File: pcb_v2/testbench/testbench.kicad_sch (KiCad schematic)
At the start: 68 parts, among them J1 test_A, J10 test_C1, J11 test_C2, J12 test_C3, J15 lcd, J17 DEBUG, J18 power_jack, J2 test_B, J3 sub_0, J4 sub_8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

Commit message: projeto enviado para impressao em dezembro/25
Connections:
- net +5V: now also J9.3 (Pin_3)
- net test_0: no longer J10.1 (Pin_1)
- net test_25: now also J10.4 (Pin_4)
- net test_26: now also J10.6 (Pin_6)
- net test_27: now also J10.8 (Pin_8)
- net test_28: now also J10.10 (Pin_10)
- net test_29: now also J10.12 (Pin_12)
- net test_30: now also J10.14 (Pin_14)
- net test_7: no longer J10.15 (Pin_15)
- net test_power_gnd_C: now also J10.15 (Pin_15); no longer J10.10 (Pin_10), J10.12 (Pin_12), J10.14 (Pin_14)
- net test_power_vcc: now also J10.1 (Pin_1); no longer J10.4 (Pin_4), J10.6 (Pin_6), J10.8 (Pin_8)
- no-connect marks 55 -> 54

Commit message: versao B2 da testbench (com a alimentacao das placas de teste reposicionadas para as extremidades
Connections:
- net mcu_power_scl: now also J9.6 (Pin_6); no longer J9.5 (Pin_5)
- net mcu_power_sda: now also J9.5 (Pin_5); no longer J9.6 (Pin_6)
- net test_0: no longer J1.1 (Pin_1), J2.1 (Pin_1)
- net test_13: no longer J1.14 (Pin_14)
- net test_21: no longer J2.22 (Pin_22)
- net test_24: no longer J1.15 (Pin_15), J2.23 (Pin_23)
- net test_31: now also J2.30 (Pin_30)
- net test_32: now also J1.23 (Pin_23), J2.31 (Pin_31)
- net test_33: now also J1.24 (Pin_24)
- net test_37: no longer J1.28 (Pin_28)
- net test_45: no longer J2.44 (Pin_44)
- net test_7: now also J2.8 (Pin_8)
- net test_8: now also J1.9 (Pin_9), J2.9 (Pin_9)
- net test_9: now also J1.10 (Pin_10)
- net test_power_gnd_A: now also J1.14 (Pin_14), J1.28 (Pin_28); no longer J1.10 (Pin_10), J1.24 (Pin_24)
- net test_power_gnd_B: now also J2.22 (Pin_22), J2.44 (Pin_44); no longer J2.31 (Pin_31), J2.9 (Pin_9)
- net test_power_vcc: now also J1.1 (Pin_1), J1.15 (Pin_15), J2.1 (Pin_1), J2.23 (Pin_23); no longer J1.23 (Pin_23), J1.9 (Pin_9), J2.30 (Pin_30), J2.8 (Pin_8)

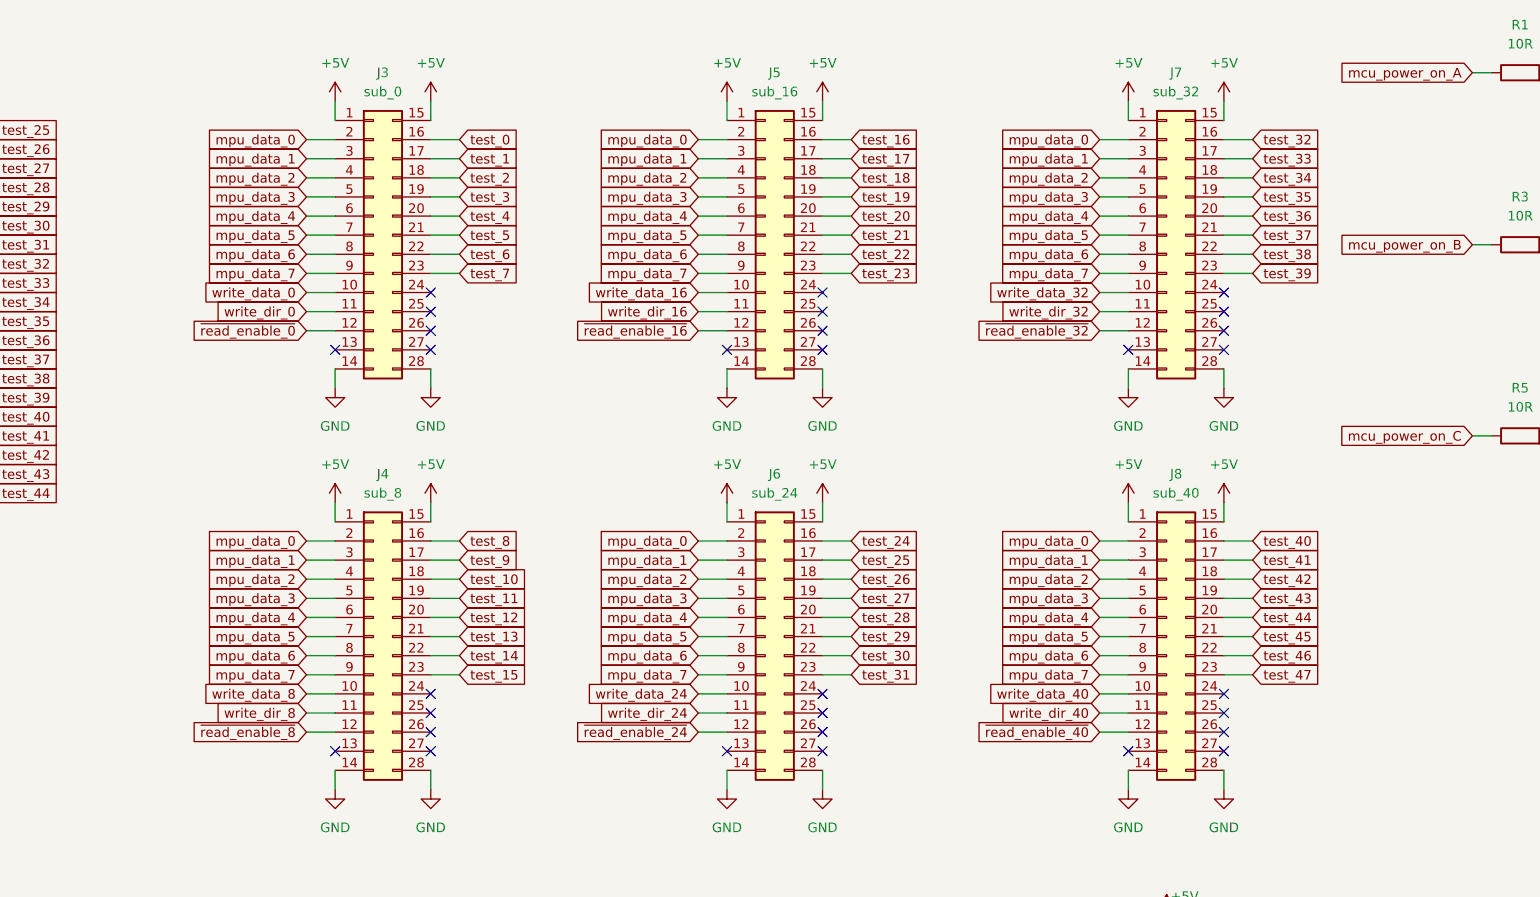
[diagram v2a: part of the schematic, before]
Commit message: a interface com a sub8 parece incompativel; corrigindo a interface
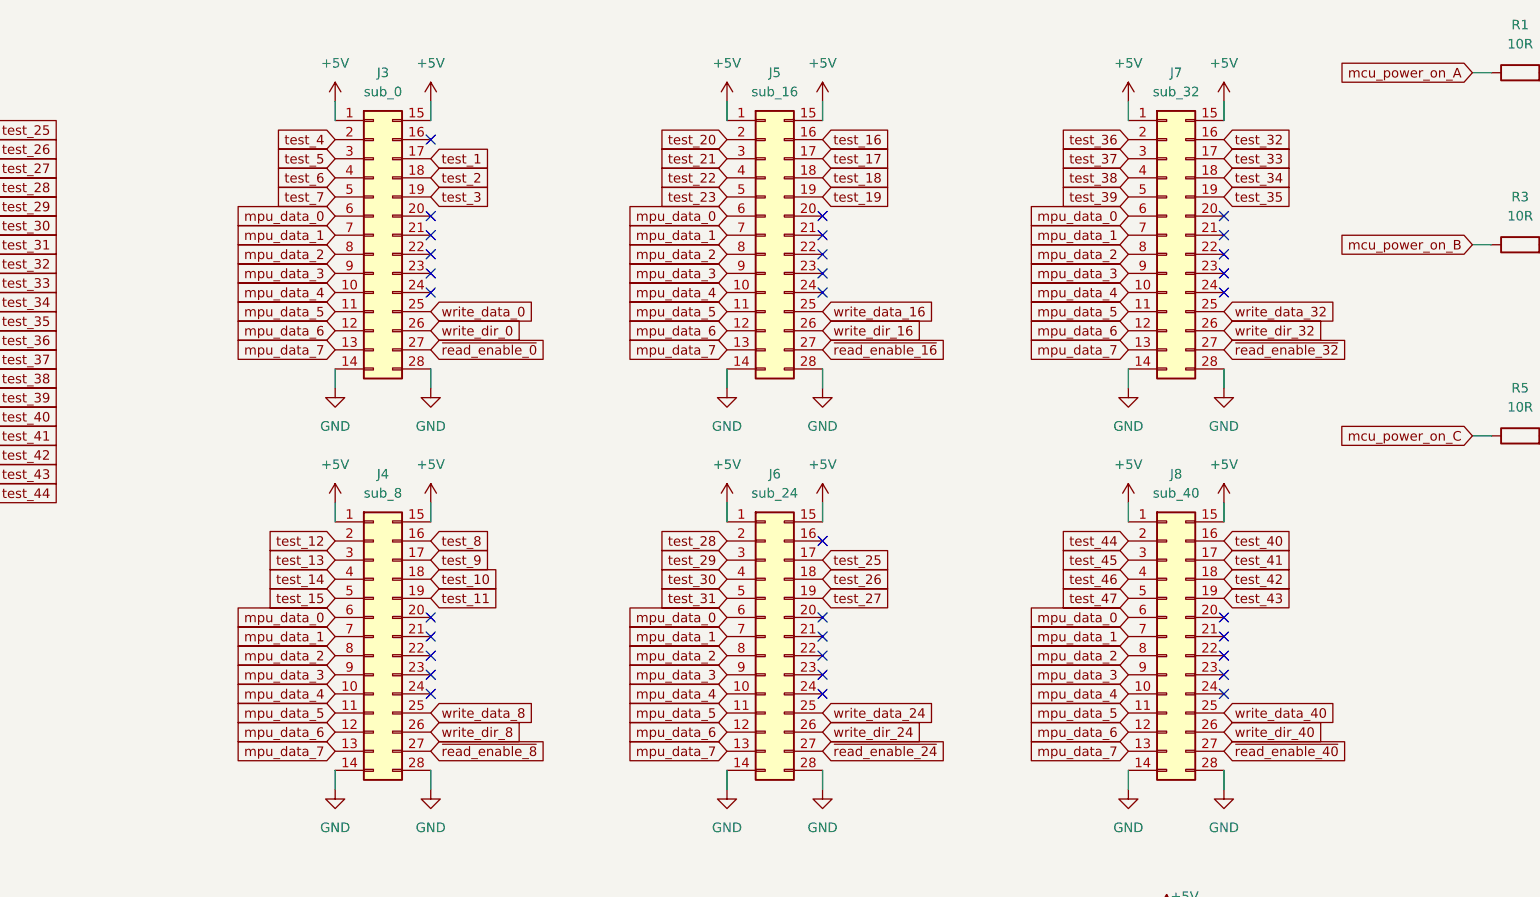
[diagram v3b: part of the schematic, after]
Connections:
- net mpu_data_0: now also J3.6 (Pin_6), J4.6 (Pin_6), J5.6 (Pin_6), J6.6 (Pin_6), J7.6 (Pin_6), J8.6 (Pin_6); no longer J3.2 (Pin_2), J4.2 (Pin_2), J5.2 (Pin_2), J6.2 (Pin_2), J7.2 (Pin_2), J8.2 (Pin_2)
- net mpu_data_1: now also J3.7 (Pin_7), J4.7 (Pin_7), J5.7 (Pin_7), J6.7 (Pin_7), J7.7 (Pin_7), J8.7 (Pin_7); no longer J3.3 (Pin_3), J4.3 (Pin_3), J5.3 (Pin_3), J6.3 (Pin_3), J7.3 (Pin_3), J8.3 (Pin_3)
- net mpu_data_2: now also J3.8 (Pin_8), J4.8 (Pin_8), J5.8 (Pin_8), J6.8 (Pin_8), J7.8 (Pin_8), J8.8 (Pin_8); no longer J3.4 (Pin_4), J4.4 (Pin_4), J5.4 (Pin_4), J6.4 (Pin_4), J7.4 (Pin_4), J8.4 (Pin_4)
- net mpu_data_3: now also J3.9 (Pin_9), J4.9 (Pin_9), J5.9 (Pin_9), J6.9 (Pin_9), J7.9 (Pin_9), J8.9 (Pin_9); no longer J3.5 (Pin_5), J4.5 (Pin_5), J5.5 (Pin_5), J6.5 (Pin_5), J7.5 (Pin_5), J8.5 (Pin_5)
- net mpu_data_4: now also J3.10 (Pin_10), J4.10 (Pin_10), J5.10 (Pin_10), J6.10 (Pin_10), J7.10 (Pin_10), J8.10 (Pin_10); no longer J3.6 (Pin_6), J4.6 (Pin_6), J5.6 (Pin_6), J6.6 (Pin_6), J7.6 (Pin_6), J8.6 (Pin_6)
- net mpu_data_5: now also J3.11 (Pin_11), J4.11 (Pin_11), J5.11 (Pin_11), J6.11 (Pin_11), J7.11 (Pin_11), J8.11 (Pin_11); no longer J3.7 (Pin_7), J4.7 (Pin_7), J5.7 (Pin_7), J6.7 (Pin_7), J7.7 (Pin_7), J8.7 (Pin_7)
- net mpu_data_6: now also J3.12 (Pin_12), J4.12 (Pin_12), J5.12 (Pin_12), J6.12 (Pin_12), J7.12 (Pin_12), J8.12 (Pin_12); no longer J3.8 (Pin_8), J4.8 (Pin_8), J5.8 (Pin_8), J6.8 (Pin_8), J7.8 (Pin_8), J8.8 (Pin_8)
- net mpu_data_7: now also J3.13 (Pin_13), J4.13 (Pin_13), J5.13 (Pin_13), J6.13 (Pin_13), J7.13 (Pin_13), J8.13 (Pin_13); no longer J3.9 (Pin_9), J4.9 (Pin_9), J5.9 (Pin_9), J6.9 (Pin_9), J7.9 (Pin_9), J8.9 (Pin_9)
- net test_12: now also J4.2 (Pin_2); no longer J4.20 (Pin_20)
- net test_13: now also J4.3 (Pin_3); no longer J4.21 (Pin_21)
- net test_14: now also J4.4 (Pin_4); no longer J4.22 (Pin_22)
- net test_15: now also J4.5 (Pin_5); no longer J4.23 (Pin_23)
- net test_20: now also J5.2 (Pin_2); no longer J5.20 (Pin_20)
- net test_21: now also J5.3 (Pin_3); no longer J5.21 (Pin_21)
- net test_22: now also J5.4 (Pin_4); no longer J5.22 (Pin_22)
- net test_23: now also J5.5 (Pin_5); no longer J5.23 (Pin_23)
- net test_28: now also J6.2 (Pin_2); no longer J6.20 (Pin_20)
- net test_29: now also J6.3 (Pin_3); no longer J6.21 (Pin_21)
- net test_30: now also J6.4 (Pin_4); no longer J6.22 (Pin_22)
- net test_31: now also J6.5 (Pin_5); no longer J6.23 (Pin_23)
- net test_36: now also J7.2 (Pin_2); no longer J7.20 (Pin_20)
- net test_37: now also J7.3 (Pin_3); no longer J7.21 (Pin_21)
- net test_38: now also J7.4 (Pin_4); no longer J7.22 (Pin_22)
- net test_39: now also J7.5 (Pin_5); no longer J7.23 (Pin_23)
- net test_4: now also J3.2 (Pin_2); no longer J3.20 (Pin_20)
- net test_44: now also J8.2 (Pin_2); no longer J8.20 (Pin_20)
- net test_45: now also J8.3 (Pin_3); no longer J8.21 (Pin_21)
- net test_46: now also J8.4 (Pin_4); no longer J8.22 (Pin_22)
- net test_47: now also J8.5 (Pin_5); no longer J8.23 (Pin_23)
- net test_5: now also J3.3 (Pin_3); no longer J3.21 (Pin_21)
- net test_6: now also J3.4 (Pin_4); no longer J3.22 (Pin_22)
- net test_7: now also J3.5 (Pin_5); no longer J3.23 (Pin_23)
- net write_data_0: now also J3.25 (Pin_25); no longer J3.10 (Pin_10)
- net write_data_16: now also J5.25 (Pin_25); no longer J5.10 (Pin_10)
- net write_data_24: now also J6.25 (Pin_25); no longer J6.10 (Pin_10)
- net write_data_32: now also J7.25 (Pin_25); no longer J7.10 (Pin_10)
- net write_data_40: now also J8.25 (Pin_25); no longer J8.10 (Pin_10)
- net write_data_8: now also J4.25 (Pin_25); no longer J4.10 (Pin_10)
- net write_dir_0: now also J3.26 (Pin_26); no longer J3.11 (Pin_11)
- net write_dir_16: now also J5.26 (Pin_26); no longer J5.11 (Pin_11)
- net write_dir_24: now also J6.26 (Pin_26); no longer J6.11 (Pin_11)
- net write_dir_32: now also J7.26 (Pin_26); no longer J7.11 (Pin_11)
- net write_dir_40: now also J8.26 (Pin_26); no longer J8.11 (Pin_11)
- net write_dir_8: now also J4.26 (Pin_26); no longer J4.11 (Pin_11)
- net ~{read_enable_0}: now also J3.27 (Pin_27); no longer J3.12 (Pin_12)
- net ~{read_enable_16}: now also J5.27 (Pin_27); no longer J5.12 (Pin_12)
- net ~{read_enable_24}: now also J6.27 (Pin_27); no longer J6.12 (Pin_12)
- net ~{read_enable_32}: now also J7.27 (Pin_27); no longer J7.12 (Pin_12)
- net ~{read_enable_40}: now also J8.27 (Pin_27); no longer J8.12 (Pin_12)
- net ~{read_enable_8}: now also J4.27 (Pin_27); no longer J4.12 (Pin_12)
- net test_0: no longer names the net of J3.16 (Pin_16)
- net test_24: no longer names the net of J6.16 (Pin_16)
- no-connect marks 54 -> 56

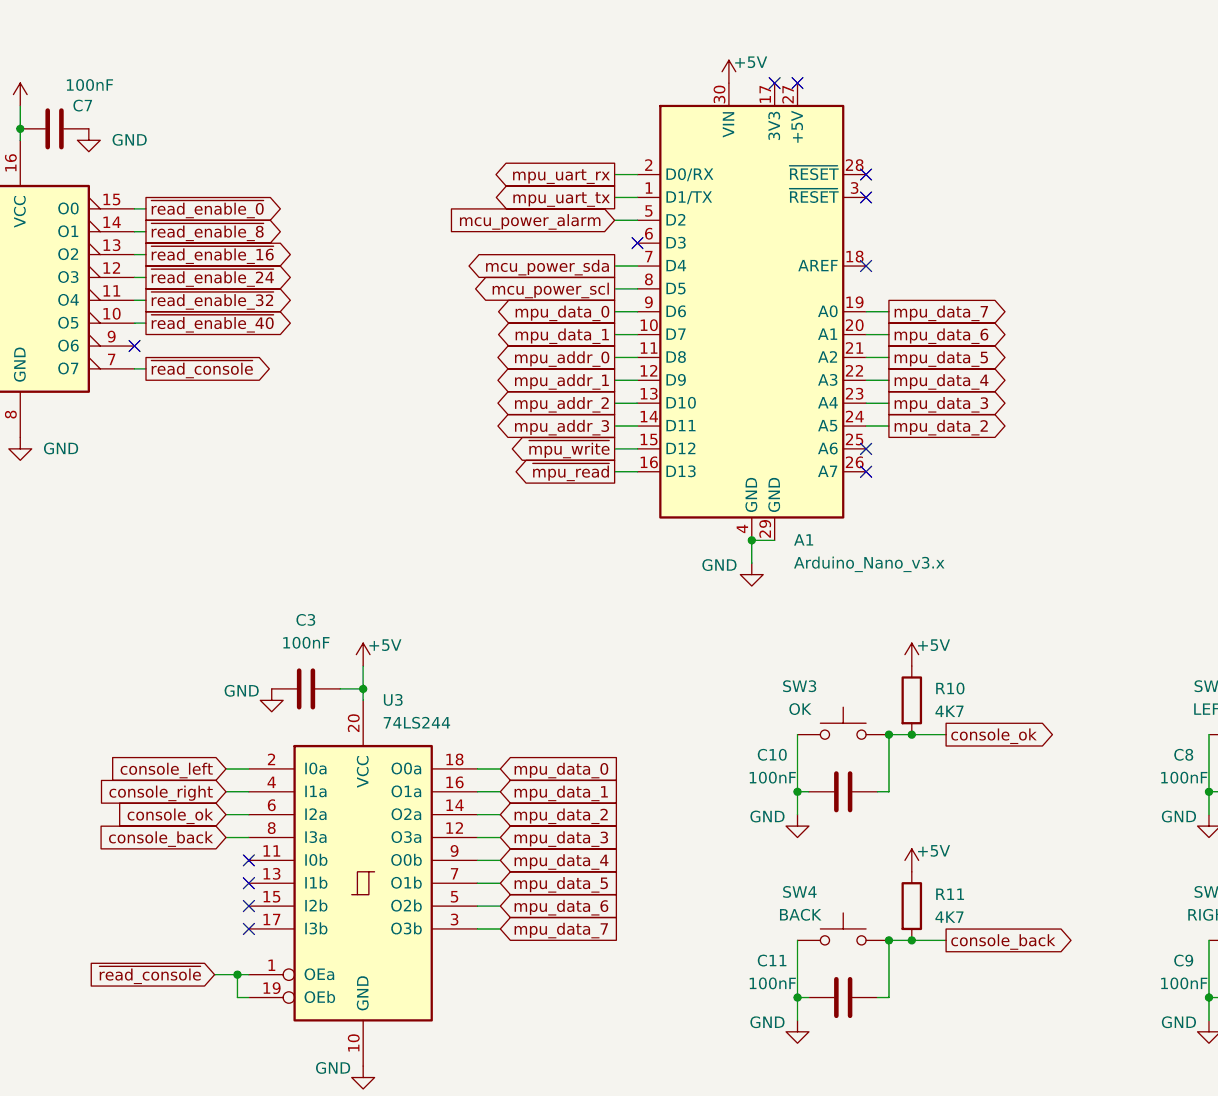
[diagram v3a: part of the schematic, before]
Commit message: correcao na pinagem do INA226 (SDA e SCL entravam nos pinos errados do arduino)
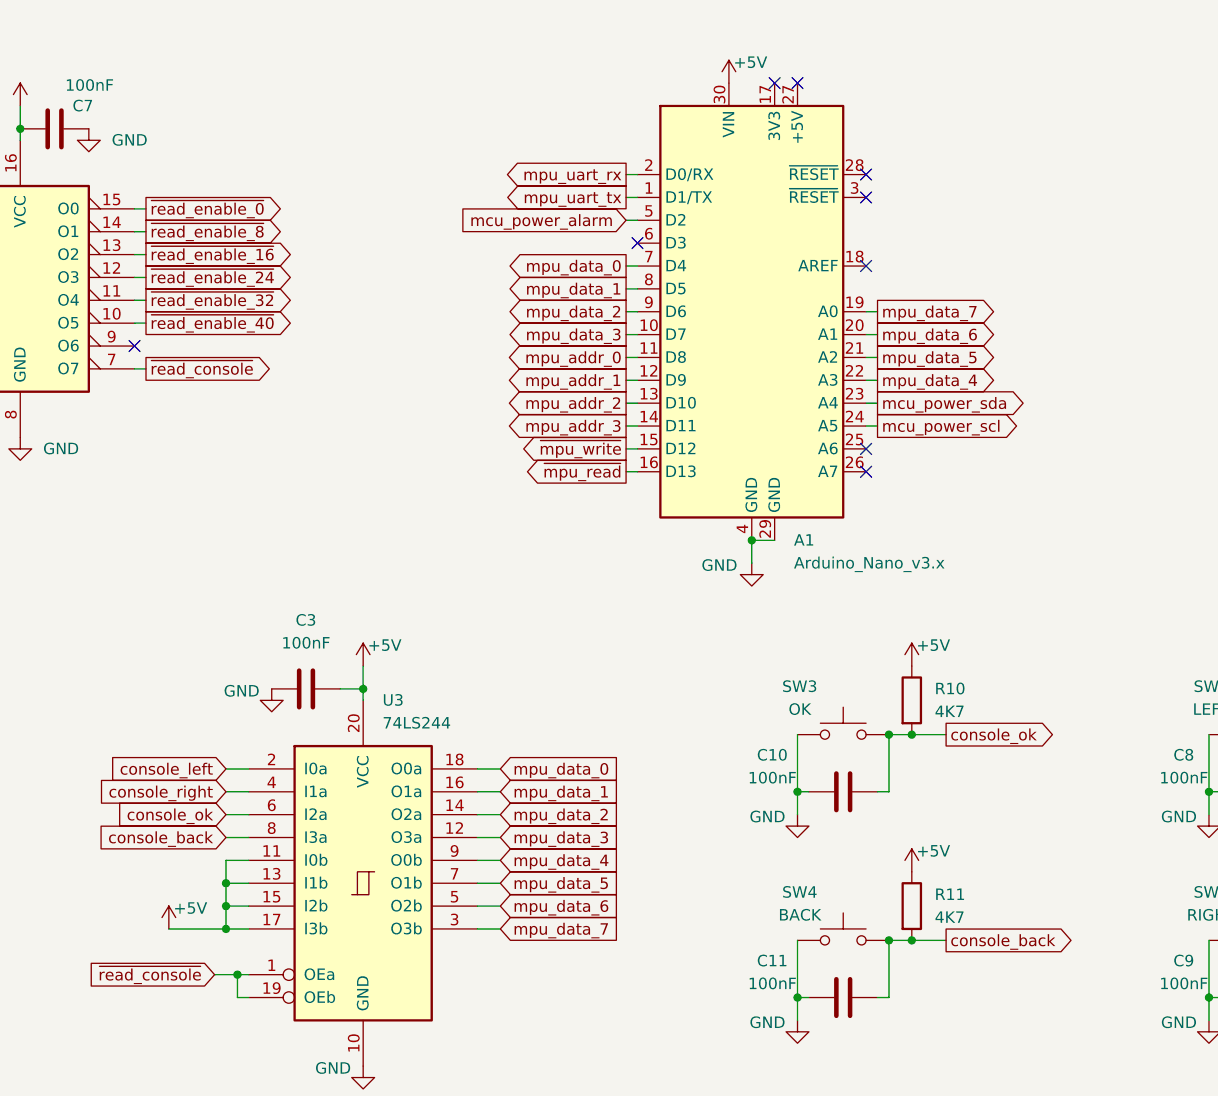
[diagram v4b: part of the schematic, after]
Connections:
- net +5V: now also U3.11 (I0b), U3.13 (I1b), U3.15 (I2b), U3.17 (I3b)
- net mcu_power_scl: now also A1.24 (A5); no longer A1.8 (D5)
- net mcu_power_sda: now also A1.23 (A4); no longer A1.7 (D4)
- net mpu_data_0: now also A1.7 (D4); no longer A1.9 (D6)
- net mpu_data_1: now also A1.8 (D5); no longer A1.10 (D7)
- net mpu_data_2: now also A1.9 (D6); no longer A1.24 (A5)
- net mpu_data_3: now also A1.10 (D7); no longer A1.23 (A4)
- no-connect marks 56 -> 52
